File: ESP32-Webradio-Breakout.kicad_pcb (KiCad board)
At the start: 2 copper layers, 118.7 x 85.1 mm, 31 parts, among them J1 Conn_01x02, J3 RCJ-042, J4 RCJ-041, Q1 BC547, SW1 RotaryEncoder_Switch, U1 ESP32NodeMCU, U2 TSR_1-2450, U3 PCF8574

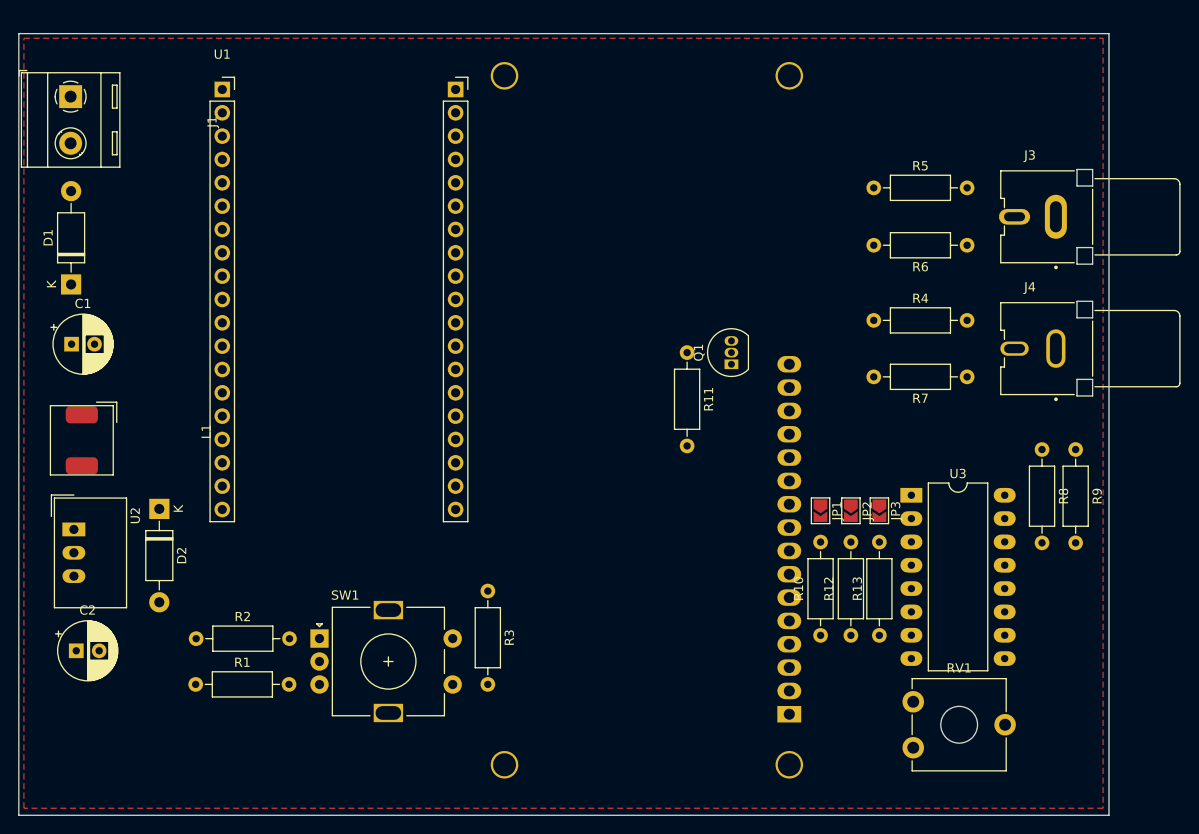
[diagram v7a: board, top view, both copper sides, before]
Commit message: adding some mounting holes and README file
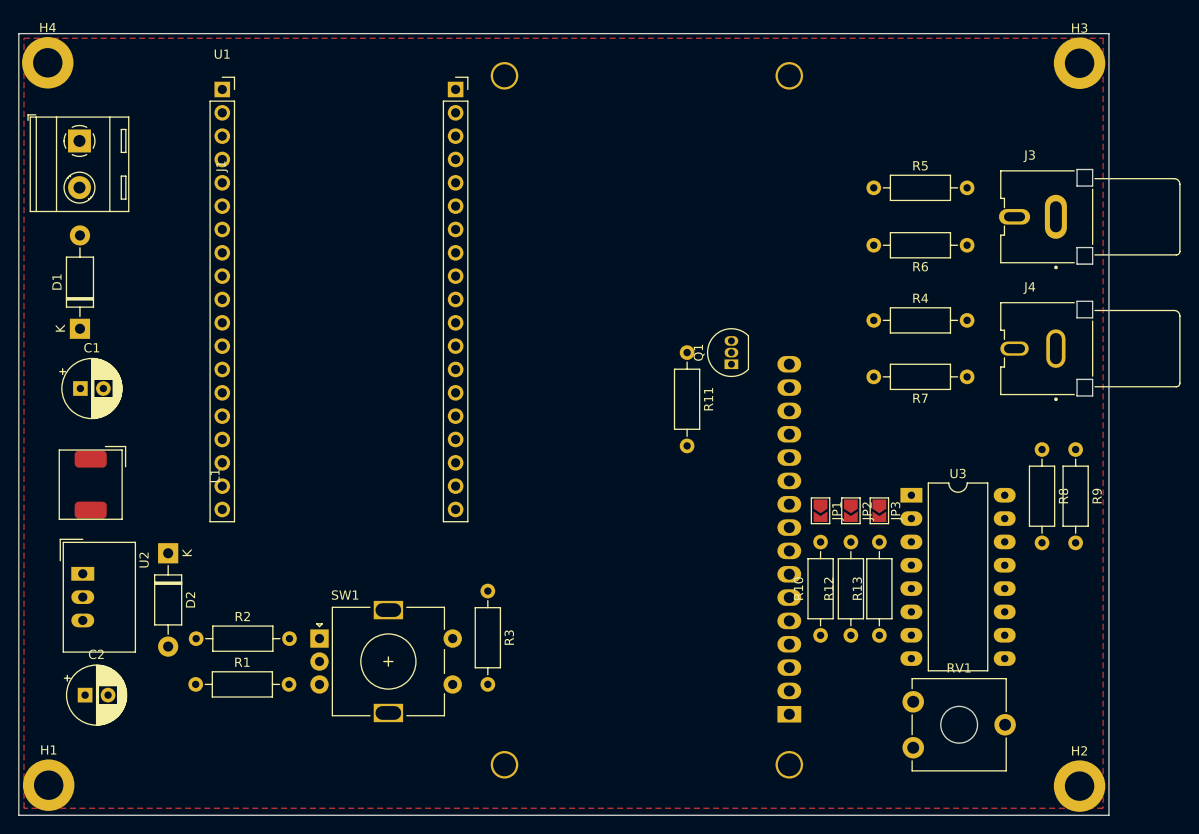
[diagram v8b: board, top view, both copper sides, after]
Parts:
- added H1: MountingHole_Pad, MountingHole:MountingHole_3.2mm_M3_DIN965_Pad, F.Cu at (99.2, 118.8)
- added H2: MountingHole_Pad, MountingHole:MountingHole_3.2mm_M3_DIN965_Pad, F.Cu at (211.4, 118.9)
- added H3: MountingHole_Pad, MountingHole:MountingHole_3.2mm_M3_DIN965_Pad, F.Cu at (211.4, 40.2)
- added H4: MountingHole_Pad, MountingHole:MountingHole_3.2mm_M3_DIN965_Pad, F.Cu at (99.1, 40.1)
- moved D2 4.92 mm to (112.2, 93.5)
- moved C1 4.92 mm to (102.7, 75.6)
- moved J1 4.92 mm to (102.6, 48.6)
- moved C2 4.92 mm to (103.2, 109.0)
- moved L1 4.92 mm to (103.8, 86.1)
- moved D1 4.92 mm to (102.6, 69.1)
- moved U2 4.92 mm to (102.9, 95.8)
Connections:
- R8 pad 2: Net-(R8-Pad2) -> /G22/SCL
- R9 pad 2: Net-(R9-Pad2) -> /G21/SDA
- U1 pad 33: unconnected-(U1-Pad33) -> /G21/SDA
- U1 pad 36: unconnected-(U1-Pad36) -> /G22/SCL
- U3 pad 14: Net-(R8-Pad2) -> /G22/SCL
- U3 pad 15: Net-(R9-Pad2) -> /G21/SDA
